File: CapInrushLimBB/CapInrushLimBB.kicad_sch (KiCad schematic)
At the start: 29 parts, among them J1 Screw_Terminal_01x02, J2 Screw_Terminal_01x02, K1 G5LE-1A, Q1 MPSA42, Q2 IRF9540N, Q3 MPSA42, Q4 BSP230 300V 0.21A

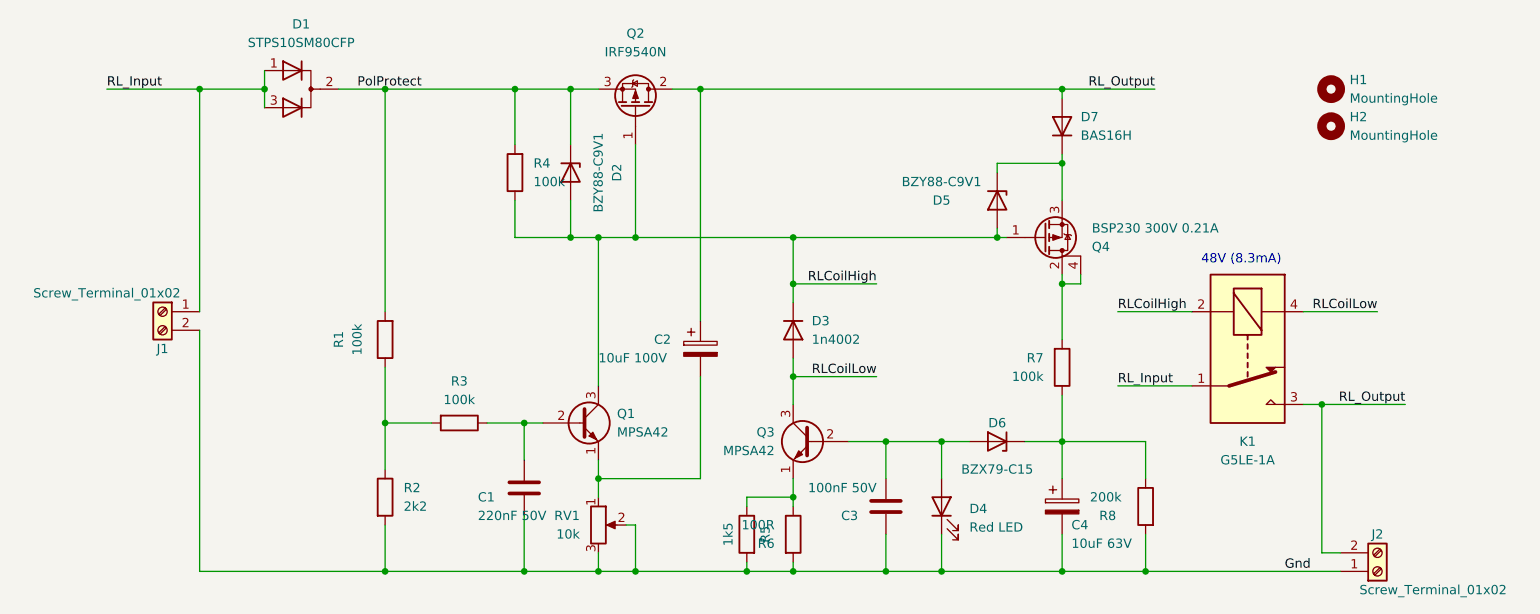
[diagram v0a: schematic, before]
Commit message: Updated to remove LED reference (use two diodes) and relayed out following update.
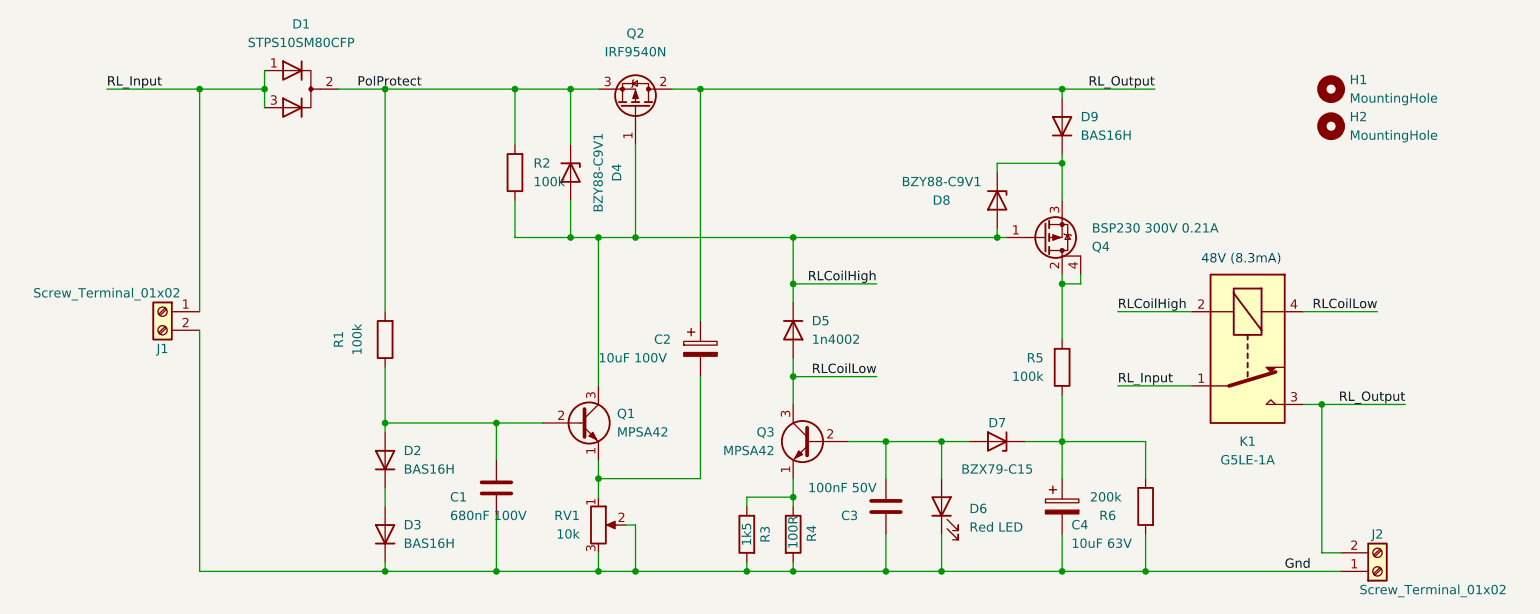
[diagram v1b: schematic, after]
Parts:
- removed R2: 2k2, Resistor_THT:R_Axial_DIN0207_L6.3mm_D2.5mm_P2.54mm_Vertical, symbol Device:R
- removed R3: 100k, Resistor_THT:R_Axial_DIN0207_L6.3mm_D2.5mm_P2.54mm_Vertical, symbol Device:R
- added D2, D3: BAS16H, Diode_SMD:D_SOD-323_HandSoldering, symbol Device:D
- C1: value 220nF 50V -> 680nF 100V
- renumbered D2 to D4, D3 to D5, D4 to D6, D6 to D7, D5 to D8, D7 to D9, R4 to R2, R5 to R3, R6 to R4, R7 to R5, R8 to R6
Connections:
- net Gnd: now also D3.1 (K)
- net at R1.1: now also C1.1, Q1.2 (B), D2.2 (A)
- new net: D2.1 (K), D3.2 (A)
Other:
- moved on the sheet: C1

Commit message: Modified schematic to support low voltage operation with 24V relay and updated board layout.
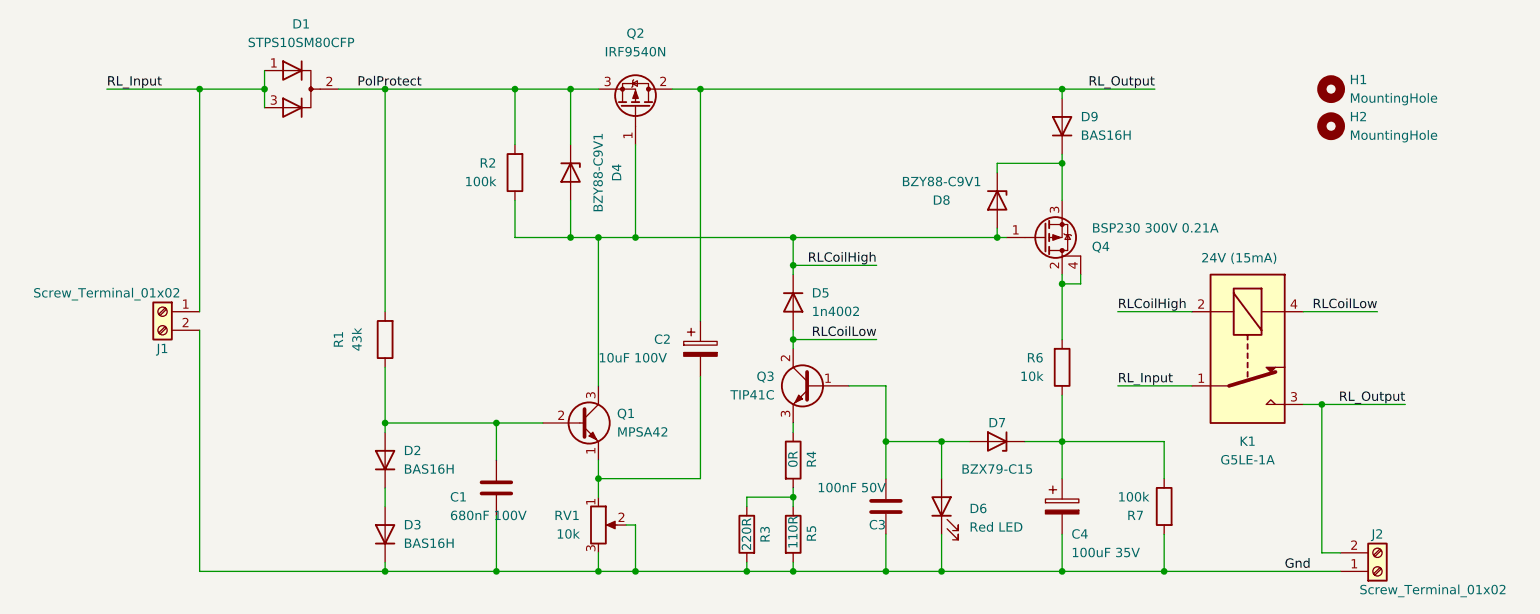
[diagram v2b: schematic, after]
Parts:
- removed Q3: MPSA42, CapInrushLim:TO-92_Inline, symbol Transistor_BJT:MPSA42
- added Q3: TIP41C, Package_TO_SOT_THT:TO-220-3_Vertical, symbol Transistor_BJT:TIP41C
- added R4: 0R, Resistor_THT:R_Axial_DIN0207_L6.3mm_D2.5mm_P2.54mm_Vertical, symbol Device:R
- C4: value 10uF 63V -> 100uF 35V; footprint Capacitor_THT:CP_Radial_D5.0mm_P2.00mm -> Capacitor_THT:CP_Radial_D6.3mm_P2.50mm
- R1: value 100k -> 43k
- R3: value 1k5 -> 220R
- R5: renamed from R4; value 100R -> 110R
- R6: renamed from R5; value 100k -> 10k
- R7: renamed from R6; value 200k -> 100k
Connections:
- net RLCoilLow: now also Q3.2 (C)
- net at R3.1, R5.1: now also R4.2
- net at C3.2, D6.2 (A), D7.2 (A): now also Q3.1 (B)
- new net: Q3.3 (E), R4.1
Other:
- note added: "24V (15mA)"
- note removed: "48V (8.3mA)"
- moved on the sheet: D5, R7

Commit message: Updated footprints in schematic and layed out tracks to make pass element accessable from the side of the board.
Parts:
- D4: footprint Diode_THT:D_DO-35_SOD27_P5.08mm_Vertical_AnodeUp -> Diode_THT:D_DO-35_SOD27_P3.81mm_Vertical_AnodeUp
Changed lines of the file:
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@@
     (property "Reference" "D4" (id 0) (at 100.33 85.09 0))
     (property "Value" "BZY88-C9V1" (id 1) (at 97.79 85.09 0))
-    (property "Footprint" "Diode_THT:D_DO-35_SOD27_P5.08mm_Vertical_AnodeUp" (id 2) (at 93.98 85.09 0)
+    (property "Footprint" "Diode_THT:D_DO-35_SOD27_P3.81mm_Vertical_AnodeUp" (id 2) (at 93.98 85.09 0)
       (effects (font (size 1.27 1.27)) hide)
     )
@@
     )
     (path "/2420062a-7b05-40e0-a967-cfdef8a9ac4f"
-      (reference "D4") (unit 1) (value "BZY88-C9V1") (footprint "Diode_THT:D_DO-35_SOD27_P5.08mm_Vertical_AnodeUp")
+      (reference "D4") (unit 1) (value "BZY88-C9V1") (footprint "Diode_THT:D_DO-35_SOD27_P3.81mm_Vertical_AnodeUp")
     )
     (path "/b236afa7-5ddc-4fa0-8b38-6e2f2c55b1a6"

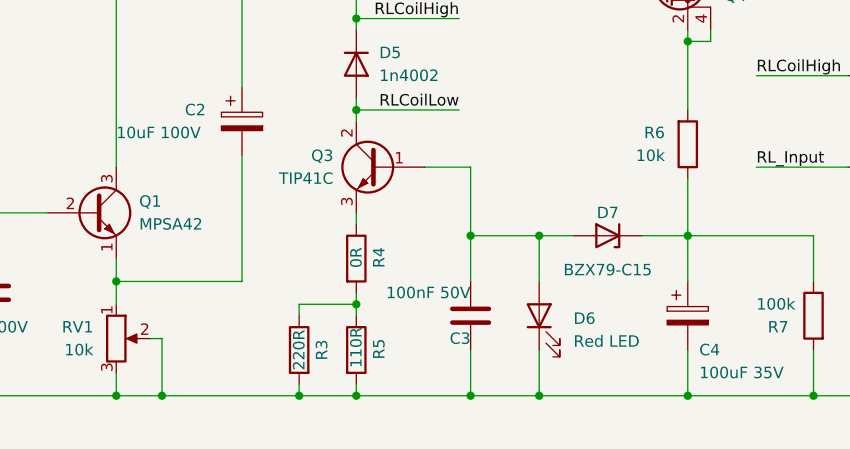
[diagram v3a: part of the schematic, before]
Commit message: Changed the reference type, changed current set resistor strategy and updated PCB.
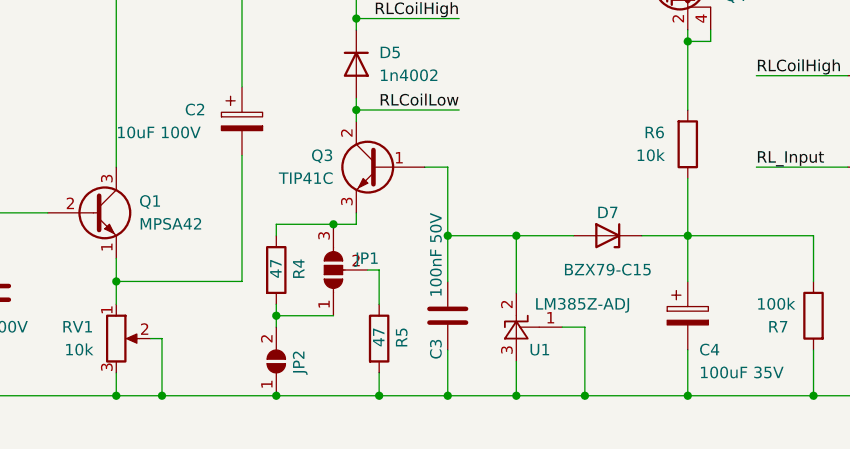
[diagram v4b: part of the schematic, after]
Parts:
- removed D6: Red LED, LED_THT:LED_D5.0mm, symbol Device:LED
- removed R3: 220R, Resistor_THT:R_Axial_DIN0207_L6.3mm_D2.5mm_P2.54mm_Vertical, symbol Device:R
- added JP1: SolderJumper_3_Open, Jumper:SolderJumper-3_P1.3mm_Open_RoundedPad1.0x1.5mm, symbol Jumper:SolderJumper_3_Open
- added JP2: SolderJumper_2_Open, Jumper:SolderJumper-2_P1.3mm_Open_RoundedPad1.0x1.5mm, symbol Jumper:SolderJumper_2_Open
- added U1: LM385Z-ADJ, CapInrushLim:TO-92_Inline, symbol Reference_Voltage:LM385Z-ADJ
- R4: value 0R -> 47
- R5: value 110R -> 47
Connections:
- net Gnd: now also JP2.1 (A), U1.1 (FB), U1.3 (A)
- net at R5.1: now also JP1.2 (C); no longer R4.2
- net at C3.2, D7.2 (A), Q3.1 (B): now also U1.2 (K)
- net at Q3.3 (E), R4.1: now also JP1.3 (B)
- new net: JP1.1 (A), JP2.2 (B), R4.2
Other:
- moved on the sheet: C3, R4, R5

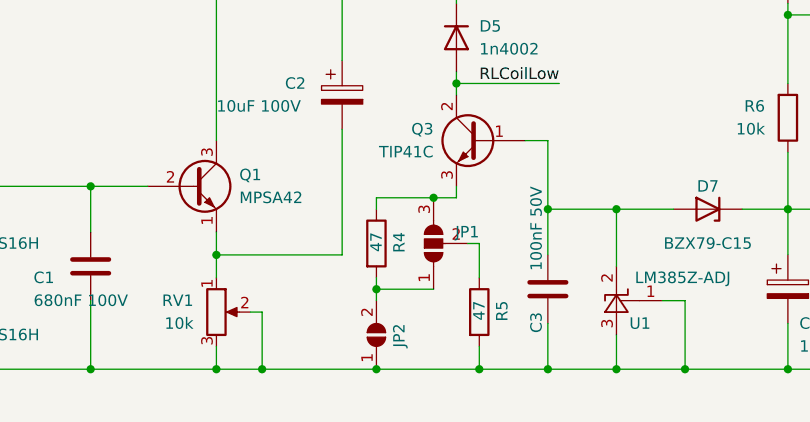
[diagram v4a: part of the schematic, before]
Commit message: Relayed out relay timer/regulator section to reduce track lengths.
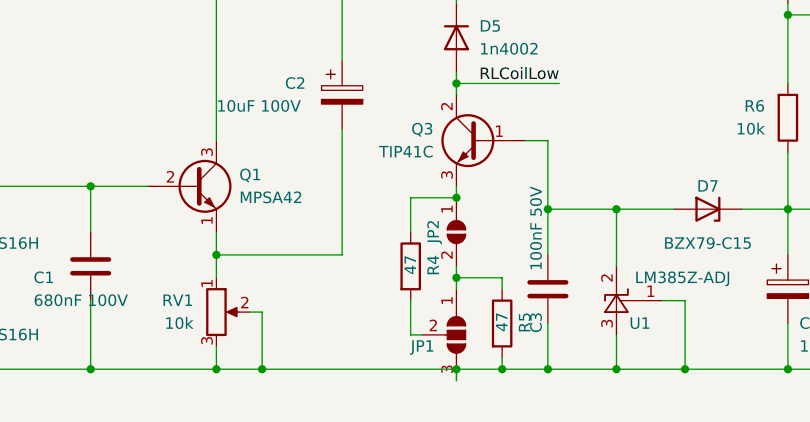
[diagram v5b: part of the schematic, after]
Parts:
- D7: footprint Diode_THT:D_DO-35_SOD27_P2.54mm_Vertical_AnodeUp -> Diode_THT:D_DO-35_SOD27_P3.81mm_Vertical_AnodeUp
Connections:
- net Gnd: now also JP1.3 (B); no longer JP2.1 (A)
- net at R5.1: now also JP1.1 (A), JP2.2 (B); no longer JP1.2 (C)
- net at Q3.3 (E), R4.1: now also JP2.1 (A); no longer JP1.3 (B)
- new net: JP1.2 (C), R4.2
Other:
- moved on the sheet: JP1, JP2, R4, R5

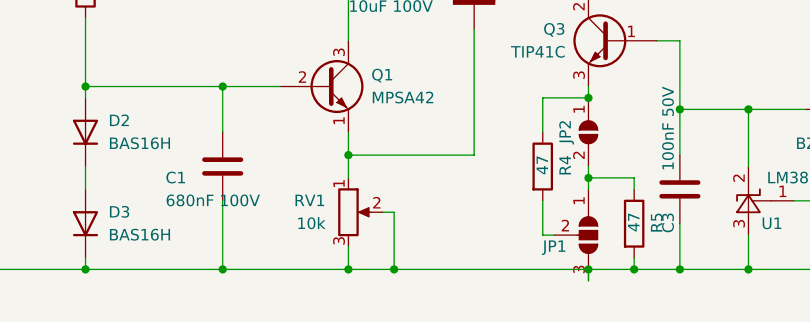
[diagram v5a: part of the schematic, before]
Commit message: Added comment text on default setting for timer pot.
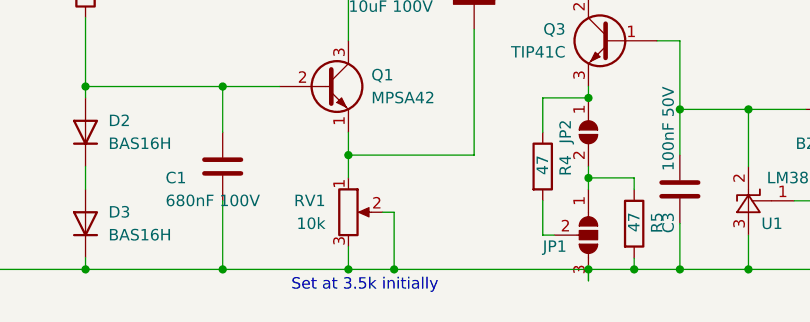
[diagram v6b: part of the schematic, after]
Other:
- note added: "Set at 3.5k initially"
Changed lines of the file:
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@@
+    (effects (font (size 1.27 1.27)) (justify left bottom))
+  )
+  (text "Set at 3.5k initially" (at 91.44 142.24 0)
     (effects (font (size 1.27 1.27)) (justify left bottom))
   )

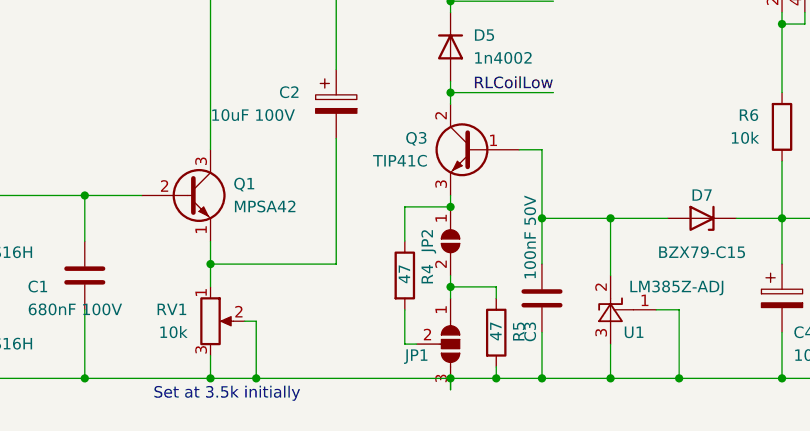
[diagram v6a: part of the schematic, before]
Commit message: Updated values of relay current limiter resistors.
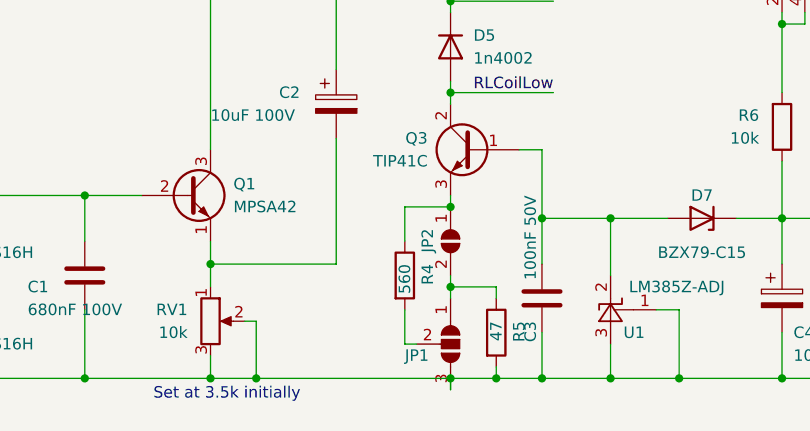
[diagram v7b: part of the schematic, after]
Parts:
- R4: value 47 -> 560
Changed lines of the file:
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@@
       (effects (font (size 1.27 1.27)) (justify right))
     )
-    (property "Value" "47" (id 1) (at 119.38 127 90)
+    (property "Value" "560" (id 1) (at 119.38 127 90)
       (effects (font (size 1.27 1.27)) (justify right))
     )
@@
     )
     (path "/c009d0ef-0fe4-4f61-a3e8-a7b3723c61b0"
-      (reference "R4") (unit 1) (value "47") (footprint "Resistor_THT:R_Axial_DIN0207_L6.3mm_D2.5mm_P2.54mm_Vertical")
+      (reference "R4") (unit 1) (value "560") (footprint "Resistor_THT:R_Axial_DIN0207_L6.3mm_D2.5mm_P2.54mm_Vertical")
     )
     (path "/145ce36a-99ab-4c24-9bc7-c0a569b41012"
